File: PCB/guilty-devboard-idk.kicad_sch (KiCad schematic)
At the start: 51 parts, among them J1 USB_C_Receptacle_USB2.0_14P, Q1 Q_NMOS, Q2 Q_PMOS, Q3 Q_PMOS, SW1 SW_Push, U1 nRF52840-CKXX, U2 SGM40567-4.2XG/TR, U3 DW01A, U4 TPS613222ADBV, U5 AD5274BCPZ-100-RL7, Y1 32MHz

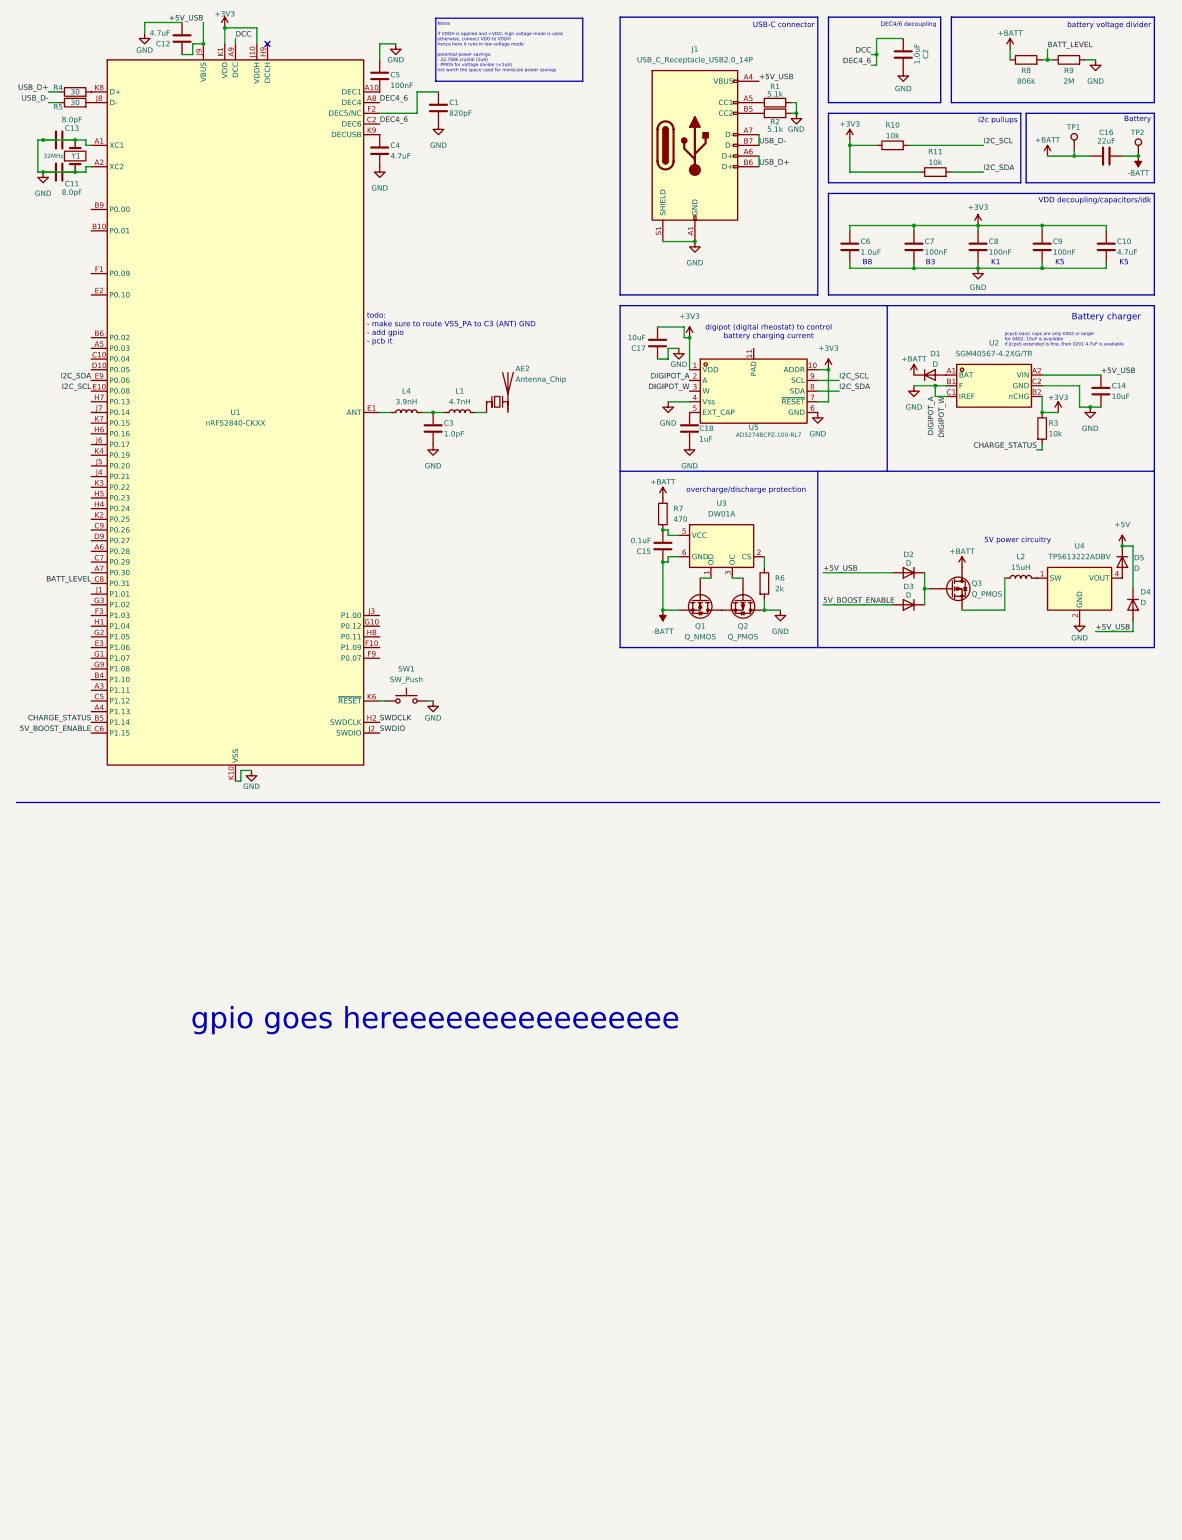
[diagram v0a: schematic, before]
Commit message: fixed power and added switch RF (dual antennas)
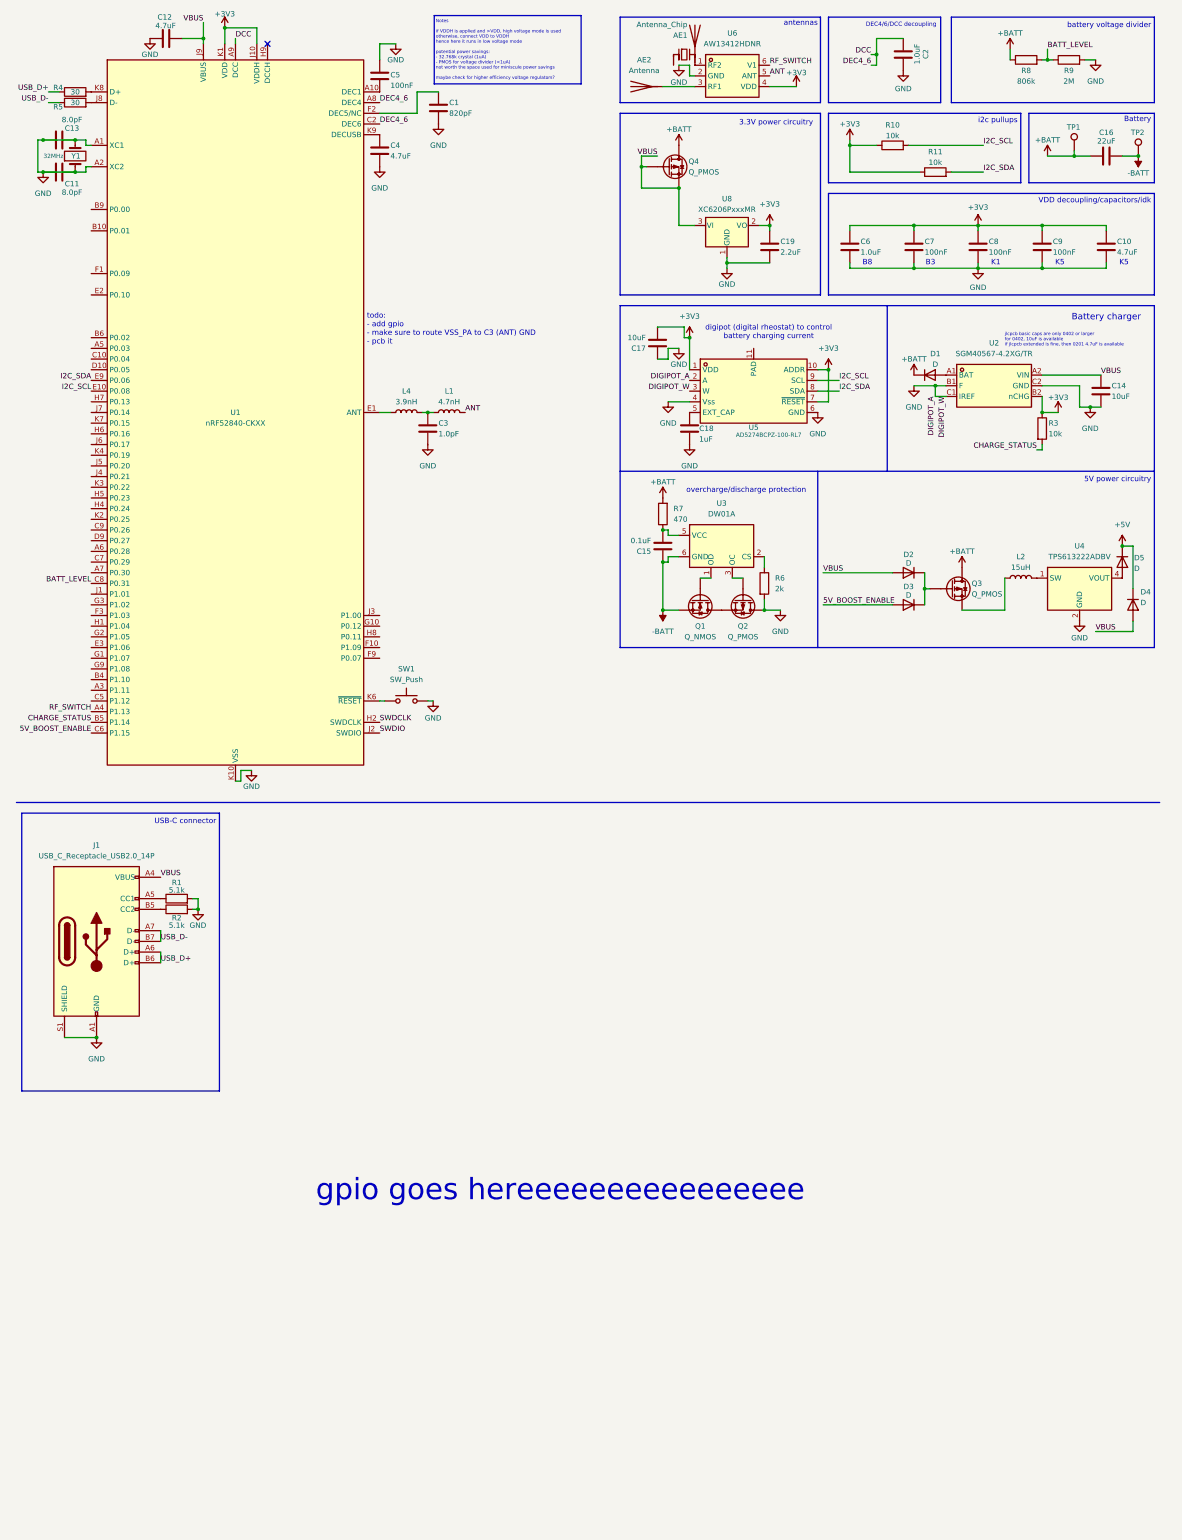
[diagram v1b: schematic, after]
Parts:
- removed AE2: Antenna_Chip, RF_Antenna:Johanson_2450AT18x100_2400-2500Mhz, symbol Device:Antenna_Chip
- added AE1: Antenna_Chip, RF_Antenna:Johanson_2450AT18x100_2400-2500Mhz, symbol Device:Antenna_Chip
- added AE2: Antenna, symbol Device:Antenna
- added C19: 2.2uF, symbol Device:C
- added Q4: Q_PMOS, symbol Device:Q_PMOS
- added U6: AW13412HDNR, easyeda2kicad:TSNP-6_L1.1-W0.7-P0.40-BL, symbol easyeda2kicad:AW13412HDNR
- added U8: XC6206PxxxMR, Package_TO_SOT_SMD:SOT-23-3, symbol Regulator_Linear:XC6206PxxxMR
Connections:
- net +3V3: now also C19.1, U6.4 (VDD), U8.2 (VO)
- net +BATT: now also Q4.D
- net GND: now also C19.2, U6.2 (GND), U8.1 (GND)
- net ANT: now reaches L1.2
- net ANT: now also U6.5 (ANT)
- net RF_SWITCH: now reaches U1.A4 (P1.13)
- net RF_SWITCH: now also U6.6 (V1)
- net +5V_USB renamed VBUS
- net VBUS: now also Q4.G, Q4.S, U8.3 (VI)
- new net: AE1.2 (PCB_Trace), U6.1 (RF2)
- new net: AE2.1 (A), U6.3 (RF1)
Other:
- note added: "3.3V power circuitry"
- note added: "DEC4/6/DCC decoupling"
- note added: "Notes if VDDH is applied and >VDD, high voltage mode is used otherwise, connect VDD to VDDH hence here it runs in low voltage mode potential power savings: - 32.768k crystal (1uA) - PMOS for voltage divider (<1uA) not worth the space used for miniscule power savings maybe check for higher efficiency voltage regulators?"
- note added: "antennas"
- note added: "todo: - add gpio - make sure to route VSS_PA to C3 (ANT) GND - pcb it"
- note removed: "DEC4/6 decoupling"
- note removed: "Notes if VDDH is applied and >VDD, high voltage mode is used otherwise, connect VDD to VDDH hence here it runs in low voltage mode potential power savings: - 32.768k crystal (1uA) - PMOS for voltage divider (<1uA) not worth the space used for miniscule power savings"
- note removed: "todo: - make sure to route VSS_PA to C3 (ANT) GND - add gpio - pcb it"
- moved on the sheet: C12, C3, J1, L1, R1, R2

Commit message: add some comments, component selection, and switch to different boost converter
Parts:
- removed L2: 15uH, symbol Device:L
- removed Q1: Q_NMOS, symbol Device:Q_NMOS
- removed Q2, Q4: Q_PMOS, symbol Device:Q_PMOS
- removed TP1, TP2: TestPoint, symbol Connector:TestPoint
- removed U4: TPS613222ADBV, Package_TO_SOT_SMD:SOT-23-5, symbol Regulator_Switching:TPS613222ADBV
- removed U8: XC6206PxxxMR, Package_TO_SOT_SMD:SOT-23-3, symbol Regulator_Linear:XC6206PxxxMR
- added C20: 22uF, Capacitor_SMD:C_0402_1005Metric, symbol Device:C
- added C21: 100nF, Capacitor_SMD:C_0201_0603Metric, symbol Device:C
- added C22: 1uF, Capacitor_SMD:C_0201_0603Metric, symbol Device:C_Small
- added D6: D, guilty-devboard-idk:0603_DSN_AND8464-D, symbol Device:D
- added D7: D, Diode_SMD:D_SOD-882, symbol Device:D
- added J3: Mirrored TCA9535 pads, Package_SO:TSSOP-24_4.4x7.8mm_P0.65mm, symbol guilty-devboard:Mirrored TCA9535PWR pads
- added L2: 2.2uH, Inductor_SMD:L_0402_1005Metric, symbol Device:L_Small
- added L3: 1.5uH, Inductor_SMD:L_0402_1005Metric, symbol Device:L
- added Q1: SP2038CNQ, easyeda2kicad:PDFN-6_L2.0-W2.0-P0.65-BL-EP-1, symbol easyeda2kicad:SP2038CNQ
- added R12: 10k, Resistor_SMD:R_0201_0603Metric, symbol Device:R
- added R13: 1M, symbol Device:R_Small
- added U4: MIC2876-5.0YMT-TR, easyeda2kicad:UDFN-8_L2.0-W2.0-P0.50-BL-EP, symbol easyeda2kicad:MIC2876-5.0YMT-TR
- added U7: TPS63031DSK, Package_SON:WSON-10-1EP_2.5x2.5mm_P0.5mm_EP1.2x2mm, symbol Regulator_Switching:TPS63031DSK
- added U8: Xiao nRF52840 Connectors, guilty-devboard-idk:Xiao nRF52840 pads, symbol guilty-devboard:Xiao nRF52840 Connectors
- AE2: footprint (none) -> Connector_Coaxial:U.FL_Molex_MCRF_73412-0110_Vertical
- C1, C10, C11, C12, C13, C15, C18, C2, C3, C4, C5, C6, C7, C8, C9: footprint (none) -> Capacitor_SMD:C_0201_0603Metric
- C14: value 10uF -> 4.7uF; footprint (none) -> Capacitor_SMD:C_0201_0603Metric
- C16: footprint (none) -> Capacitor_SMD:C_0402_1005Metric
- C17: value 10uF -> 0.1uF; footprint (none) -> Capacitor_SMD:C_0201_0603Metric
- C19: value 2.2uF -> 22uF; footprint (none) -> Capacitor_SMD:C_0402_1005Metric
- D1, D2, D3: footprint (none) -> Diode_SMD:D_SOD-882
- D4: footprint (none) -> Diode_SMD:D_SOD-123
- D5: footprint (none) -> guilty-devboard-idk:0603_DSN_AND8464-D
- L1, L4: footprint (none) -> Inductor_SMD:L_0201_0603Metric
- Q2: renamed from Q3; footprint (none) -> Inductor_SMD:L_0603_1608Metric
- R1, R10, R11, R2, R3, R4, R5, R6, R7, R9: footprint (none) -> Resistor_SMD:R_0201_0603Metric
- R8: footprint (none) -> Resistor_SMD:R_0402_1005Metric
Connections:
- net +3V3: now also R12.1, R13.2, U7.1 (VOUT), U7.10 (FB), U8.10 (3V3)
- net +5V: now also U8.8 (5V)
- net +BATT: now also C16.2, D6.2 (A), U8.16 (BAT+); no longer C16.1
- net -BATT: now also C16.1, Q1.1 (S1), U8.15 (BAT-); no longer C16.2
- net I2C_SCL: now also U8.6 (SCL_D5)
- net I2C_SDA: now also U8.5 (SDA_D4)
- net SWDCLK: now also U8.20 (CLK)
- net SWDIO: now also U8.19 (DIO)
- net VBUS: now also D7.2 (A)
- net at U3.1 (OD): now also Q1.2 (G1)
- net at U3.3 (OC): now also Q1.5 (G2)
- net at D5.2 (A): now also C20.2, U4.5 (OUTS), U4.8 (OUT)
- net AGND: now reaches SW1.1
- net AGND: now also C1.2, C10.2, C11.1, C11.2, C12.1, C13.1, C13.2, C14.2, C17.1, C18.1, C19.2, C2.2, C3.1, C4.2, C5.1, C6.2, C7.2, C8.2, C9.2, J1.A1 (GND), J1.A12 (GND), J1.B1 (GND), J1.B12 (GND), J1.S1 (SHIELD), R1.2, R2.2, R6.2, R9.2, U1.A1 (XC1), U1.A2 (XC2), U1.B7 (VSS), U1.C1 (VSS_PA), U1.C4 (VSS), U1.D3 (VSS), U1.D4 (VSS), U1.D5 (VSS), U1.D6 (VSS), U1.D7 (VSS), U1.D8 (VSS), U1.E4 (VSS), U1.E5 (VSS), U1.E6 (VSS), U1.E7 (VSS), U1.E8 (VSS), U1.F4 (VSS), U1.F5 (VSS), U1.F6 (VSS), U1.F7 (VSS), U1.F8 (VSS), U1.G4 (VSS), U1.G5 (VSS), U1.G6 (VSS), U1.G7 (VSS), U1.G8 (VSS), U1.K10 (VSS), U2.B1 (F), U2.C1 (IREF), U2.C2 (GND), U5.2 (A), U5.3 (W), U5.4 (Vss), U5.6 (GND), U6.2 (GND), Y1.1, Y1.2, C20.1, C21.2, C22.1, Q1.3 (D2), U4.2 (PGND), U4.4 (AGND), U4.9 (EP), U7.11 (PGND), U7.3 (PGND), U7.9 (GND), U8.22 (GND), U8.9 (GND); no longer U1.K6 (~{RESET})
- net at Q2.S: now also C22.2, L2.1, U4.3 (IN), U4.6 (EN)
- net P0.03_AIN1: now reaches U1.A5 (P0.03)
- net P0.03_AIN1: now also U8.2 (A/D1)
- net P0.02_AIN0: now reaches U1.B6 (P0.02)
- net P0.02_AIN0: now also U8.1 (A/D0)
- net P0.04_AIN2: now reaches U1.C10 (P0.04)
- net P0.04_AIN2: now also U8.3 (A/D2)
- net 5V_POWER_GOOD: now reaches U1.C5 (P1.12)
- net 5V_POWER_GOOD: now also R13.1, U4.7 (/PG)
- net P0.05_AIN3: now reaches U1.D10 (P0.05)
- net P0.05_AIN3: now also U8.4 (A/D3)
- removed net GND: C1.2, C10.2, C11.1, C11.2, C12.1, C13.1, C13.2, C14.2, C17.1, C18.1, C19.2, C2.2, C3.1, C4.2, C5.1, C6.2, C7.2, C8.2, C9.2, J1.A1 (GND), J1.A12 (GND), J1.B1 (GND), J1.B12 (GND), J1.S1 (SHIELD), R1.2, R2.2, R6.2, R9.2, SW1.2, U1.A1 (XC1), U1.A2 (XC2), U1.B7 (VSS), U1.C1 (VSS_PA), U1.C4 (VSS), U1.D3 (VSS), U1.D4 (VSS), U1.D5 (VSS), U1.D6 (VSS), U1.D7 (VSS), U1.D8 (VSS), U1.E4 (VSS), U1.E5 (VSS), U1.E6 (VSS), U1.E7 (VSS), U1.E8 (VSS), U1.F4 (VSS), U1.F5 (VSS), U1.F6 (VSS), U1.F7 (VSS), U1.F8 (VSS), U1.G4 (VSS), U1.G5 (VSS), U1.G6 (VSS), U1.G7 (VSS), U1.G8 (VSS), U1.K10 (VSS), U2.B1 (F), U2.C1 (IREF), U2.C2 (GND), U5.2 (A), U5.3 (W), U5.4 (Vss), U5.6 (GND), U6.2 (GND), Y1.1, Y1.2
- new net: L2.2, U4.1 (SW)
- new net: Q1.4 (S2), Q1.6 (D1)
- new net: D6.1 (K), D7.1 (K), U7.5 (VIN), U7.6 (EN), U7.7 (PS/SYNC), U7.8 (VINA)
- new net: L3.1, U7.2 (L2)
- new net: L3.2, U7.4 (L1)
- new net RESET: C21.1, R12.2, SW1.2, U1.K6 (~{RESET}), U8.21 (RST)
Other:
- note added: "AGND and GND should be connected at one spot"
- note added: "AGND-GND"
- note added: "Battery pads"
- note added: "Notes if VDDH is applied and >VDD, high voltage mode is used otherwise, connect VDD to VDDH hence here it runs in low voltage mode potential power savings: - 32.768k crystal (1uA) - PMOS for voltage divider (<1uA) not worth the space used for miniscule power savings - maybe check for higher efficiency 3.3v regulators? - maybe remove 5V_PG - maybe add recommended VIN cap near 5V reg"
- note added: "TODO: switch to nrf52840 plus clone still working on that symbol and footprint (also connect the rest of the GPIO lol)"
- note added: "capacitors should be as close as possible"
- note added: "connect /PG to AGND if unused"
- note added: "could use EN pin to enable/disable, but only accepts up to VIN, and if on USB, then VBUS is applied, and VBUS > VIN so to make it work would require running USB through it, which would be more complex and more inefficient to make it work at all would take more components than it saves"
- note added: "maybe add an easier to access swdio/swdclk thing? at least if there's space"
- note added: "note 4.8A switching current != 4.8A output current absolute theoretical max ~2.5A output current this diode is only rated for 2A and i only guarantee 1A based off datahseet"
- note added: "recommended 4.7+ uF ^^^ capacitor here as close as possible to inductor and connected to PGND, but not required"
- note added: "so you can design a PCB using this such that you can swap it out for a standard xiao and lose minimal functionality"
- note added: "todo: - add the rest of the gpio - make sure to route VSS_PA to C3 (ANT) GND - pcb it"
- note removed: "Battery"
- note removed: "Notes if VDDH is applied and >VDD, high voltage mode is used otherwise, connect VDD to VDDH hence here it runs in low voltage mode potential power savings: - 32.768k crystal (1uA) - PMOS for voltage divider (<1uA) not worth the space used for miniscule power savings maybe check for higher efficiency voltage regulators?"
- note removed: "jlcpcb basic caps are only 0402 or larger for 0402, 10uF is available if jlcpcb extended is fine, then 0201 4.7uF is available"
- note removed: "todo: - add gpio - make sure to route VSS_PA to C3 (ANT) GND - pcb it"
- moved on the sheet: C1, C10, C16, C19, C6, C7, C8, C9, D2, D3, D4, D5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
